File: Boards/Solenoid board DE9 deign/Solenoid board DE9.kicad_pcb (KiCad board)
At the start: 2 copper layers, 190.6 x 177.9 mm, 4 parts, among them J2 DE9_Receptacle_MountingHoles

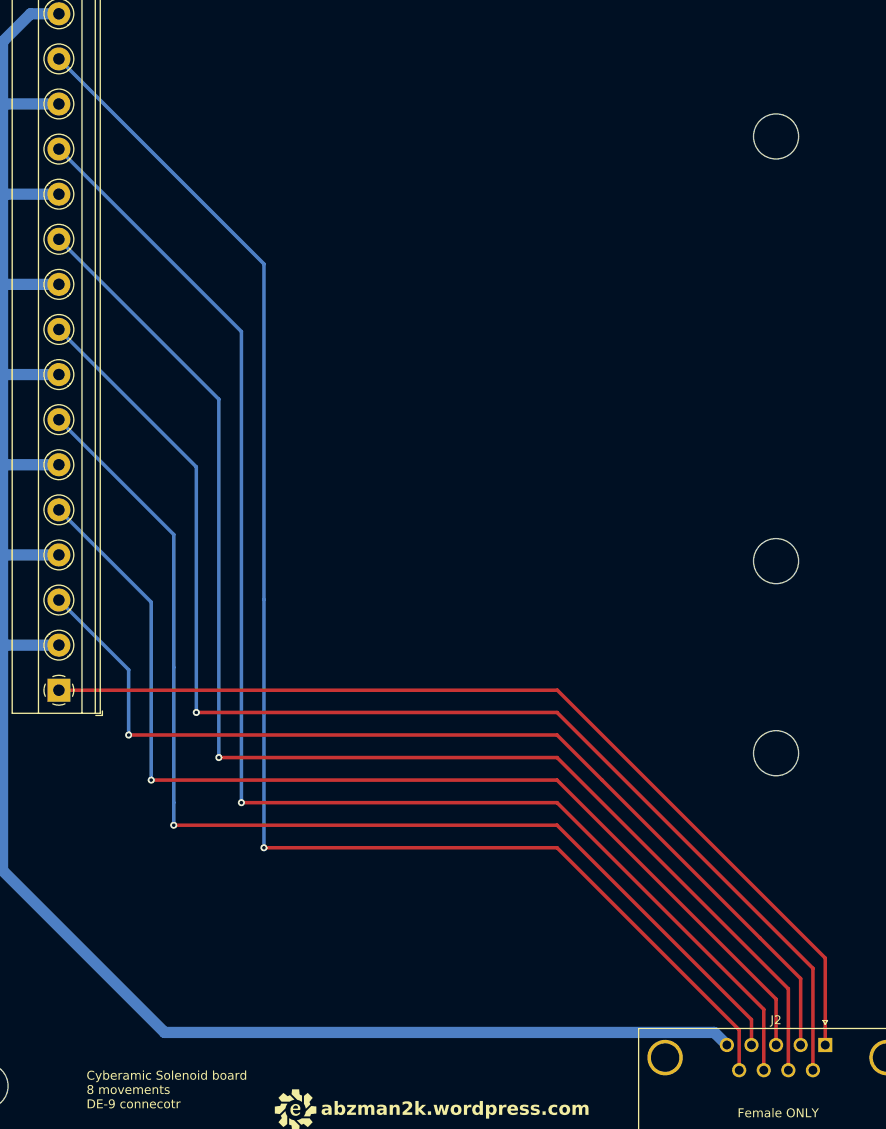
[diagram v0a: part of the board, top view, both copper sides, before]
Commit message: added audio board schematics and de9 board fab files
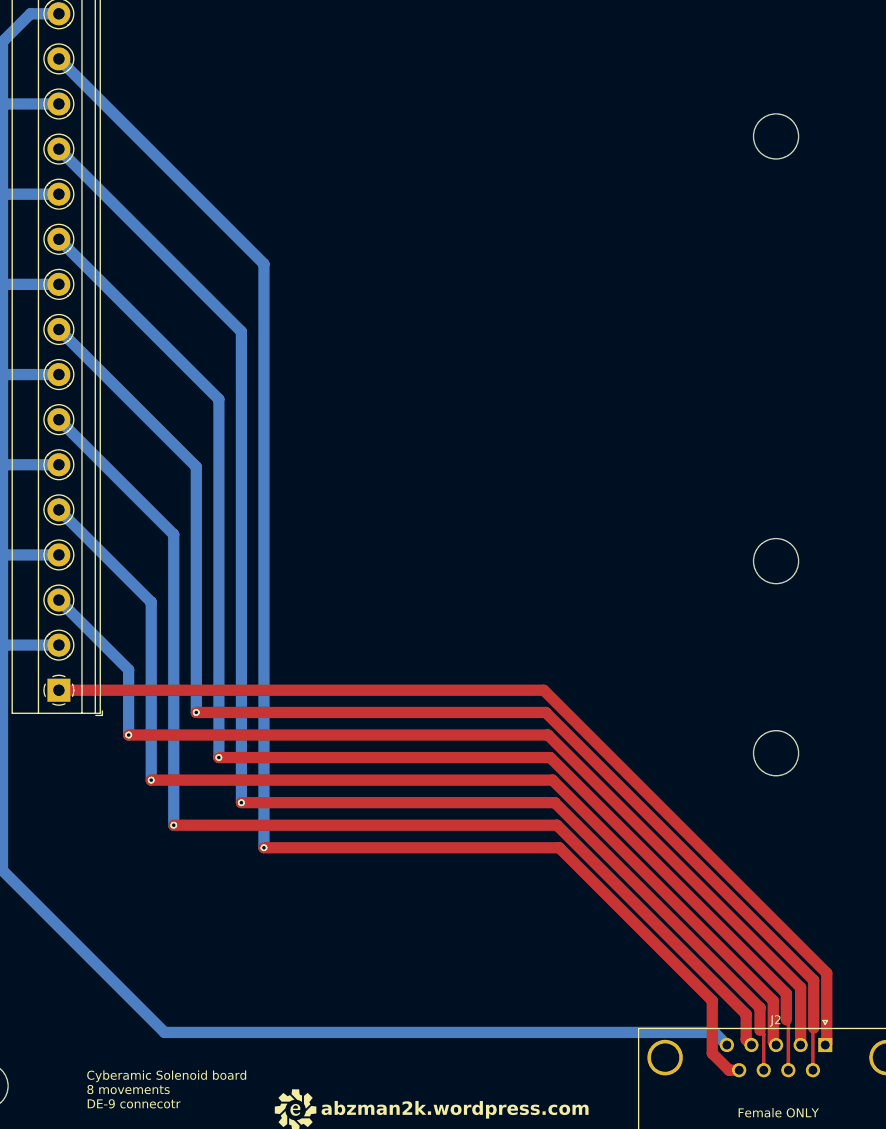
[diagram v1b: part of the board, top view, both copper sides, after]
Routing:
- net CC8: track 165.0 -> 165.8 mm
- net CC1: track 108.6 -> 107.9 mm
- net CC5: track 142.4 -> 141.8 mm
- net CC2: track 113.0 -> 112.4 mm
